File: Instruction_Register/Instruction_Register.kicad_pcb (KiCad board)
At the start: 2 copper layers, 95.9 x 90.2 mm, 24 parts, among them J1 Conn_01x12, J2 Conn_01x16, U1 74LS245, U2 74LS173, U3 74LS173

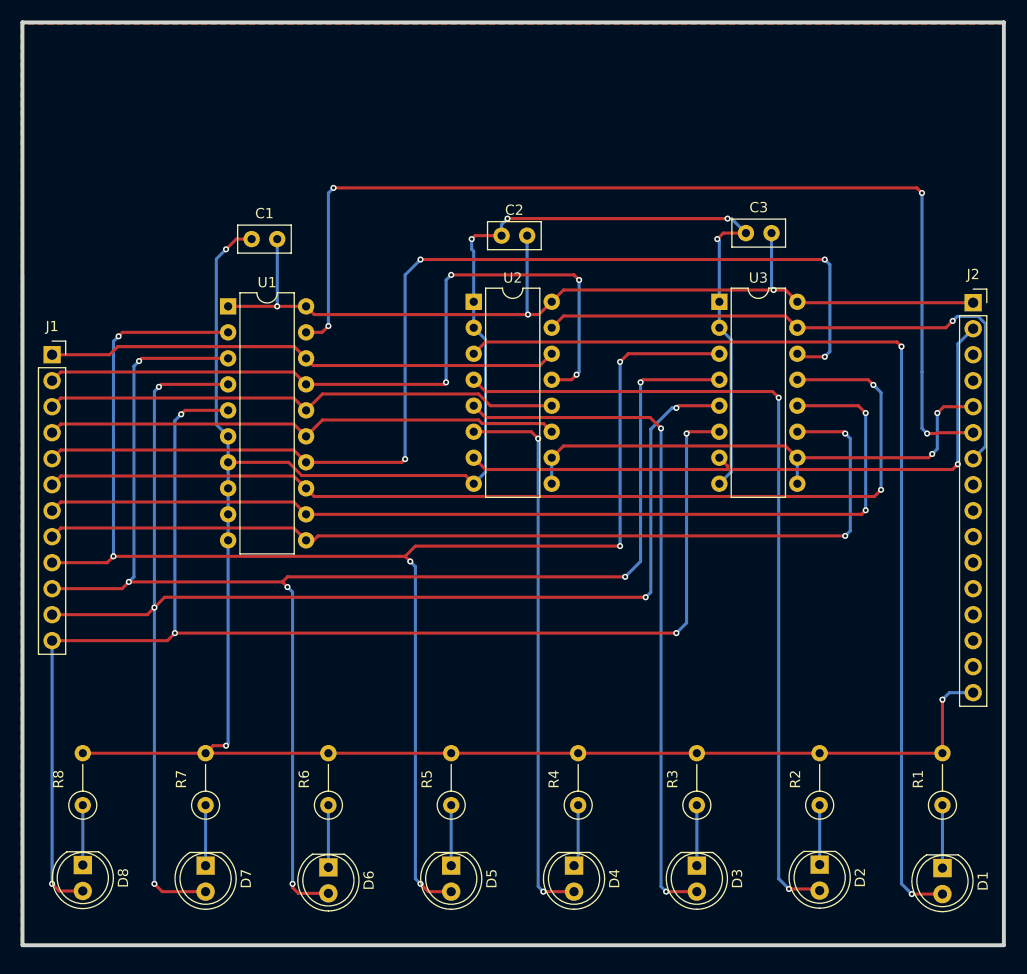
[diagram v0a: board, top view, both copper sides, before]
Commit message: returning to pc104 standard
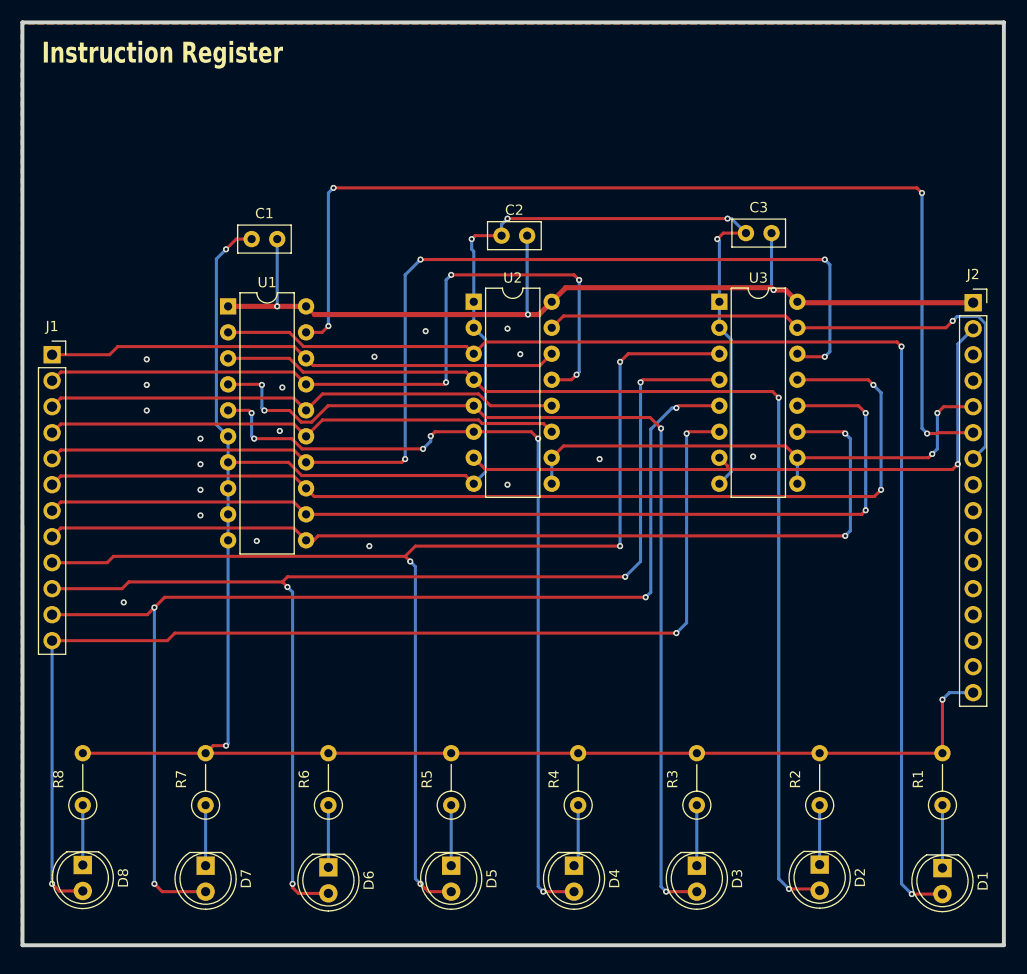
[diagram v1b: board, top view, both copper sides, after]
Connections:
- U1 pad 2: /ir4 -> Net-(D1-A)
- U1 pad 3: /ir5 -> Net-(D2-A)
- U1 pad 4: /ir6 -> Net-(D3-A)
- U1 pad 5: /ir7 -> Net-(D4-A)
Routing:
- net /ir4: track 152.7 -> 120.1 mm, vias 6 -> 4
- net /ir5: track 148.7 -> 117.9 mm, vias 6 -> 4
- net /ir6: track 143.9 -> 115.3 mm, vias 5 -> 4
- net Net-(D4-A): track 54.1 -> 81.9 mm, vias 2 -> 6
- net Net-(D3-A): track 67.7 -> 95.2 mm, vias 2 -> 4
- net /ir7: track 137.9 -> 111.5 mm, vias 5 -> 3
- net Net-(D1-A): track 99.4 -> 124.2 mm
- net Net-(D2-A): track 82.0 -> 106.6 mm
- net Net-(D4-K): track 6.08 -> 5.50 mm
- net GND: vias 7 -> 26
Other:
- board text added: "Instruction Register"

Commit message: updated instruction register to match pc104
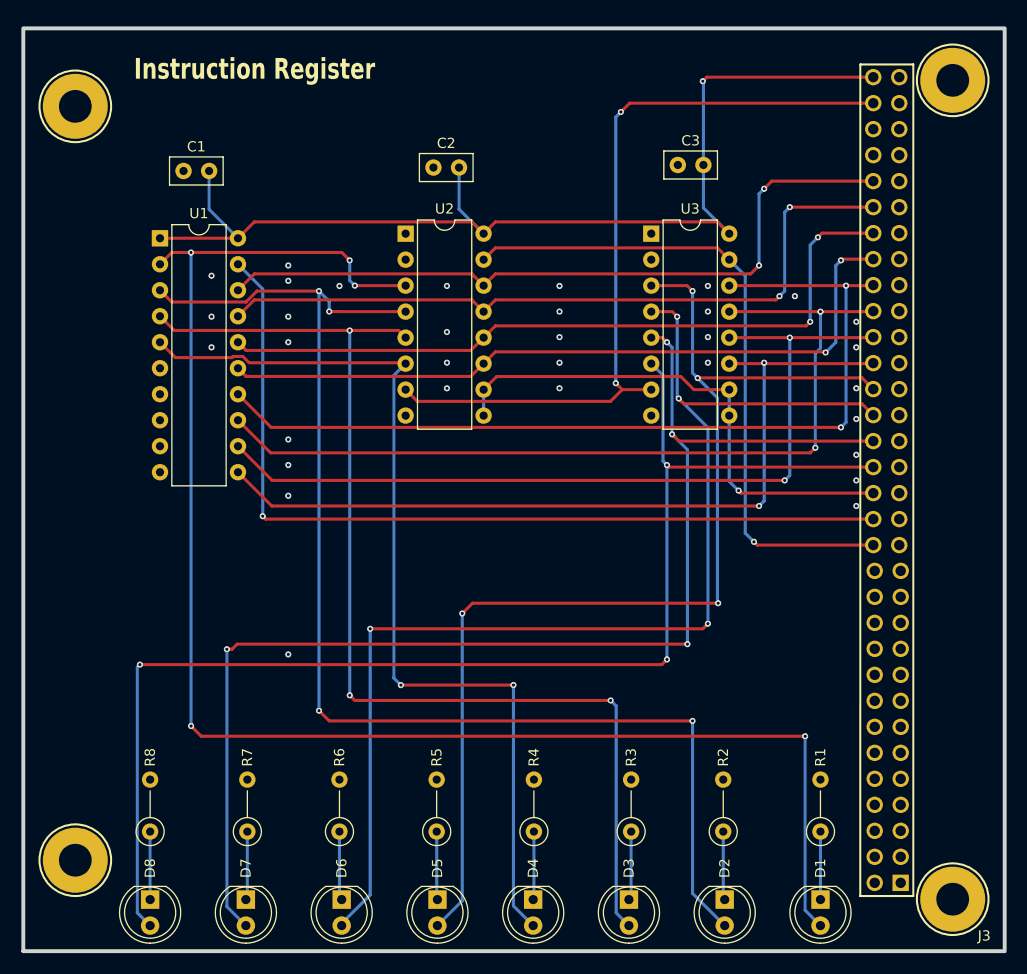
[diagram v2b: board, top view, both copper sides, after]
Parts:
- removed J1: Conn_01x12, Connector_PinSocket_2.54mm:PinSocket_1x12_P2.54mm_Vertical
- removed J2: Conn_01x16, Connector_PinSocket_2.54mm:PinSocket_1x16_P2.54mm_Vertical
- added J3: ~, MyFootPrints:PC104-Standard, F.Cu at (199.0, 145.2)
- moved D1 12.3 mm to (181.0, 140.2)
- moved R1 12.2 mm to (181.0, 133.6)
- moved D2 9.89 mm to (171.6, 140.2)
- moved R2 9.77 mm to (171.5, 133.6)
- moved C1 9.41 mm to (118.7, 69.0)
- moved U1 9.41 mm to (116.4, 75.6)
- moved U2 9.41 mm to (140.4, 75.1)
- moved U3 9.41 mm to (164.4, 75.1)
- moved C2 9.41 mm to (143.2, 68.7)
- moved C3 9.41 mm to (167.0, 68.4)
- moved D3 7.42 mm to (162.3, 140.2)
- moved D8 7.40 mm to (115.5, 140.2)
- moved R8 7.07 mm to (115.5, 133.6)
- moved R3 6.92 mm to (162.5, 133.6)
- moved D4 5.19 mm to (152.9, 140.2)
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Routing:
- net GND: track 253.8 -> 0.00 mm, vias 26 -> 33
- net Net-(D1-A): track 124.2 -> 152.8 mm, vias 2 -> 5
- net /bus0: track 50.4 -> 71.5 mm, vias 0 -> 2
- net /bus3: track 50.8 -> 71.6 mm, vias 0 -> 2
- net /bus2: track 50.8 -> 71.5 mm, vias 0 -> 2
- net /bus4: track 107.4 -> 88.4 mm, vias 4 -> 2
- net Net-(D2-A): track 106.6 -> 125.6 mm, vias 2 -> 4
- net /~{ir_oe}: track 102.1 -> 85.4 mm, vias 4 -> 1
- net /ir7: track 111.5 -> 127.6 mm
- net /bus5: track 100.7 -> 85.5 mm
- net /clock: track 63.3 -> 77.6 mm, vias 1 -> 2
- net /bus6: track 97.0 -> 83.1 mm
- net Net-(D3-A): track 95.2 -> 109.0 mm, vias 4 -> 3
- net /bus7: track 93.7 -> 80.6 mm
- net 5V: track 94.2 -> 105.7 mm, vias 3 -> 1
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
